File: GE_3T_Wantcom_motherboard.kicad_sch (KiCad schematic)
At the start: 27 parts, among them J1 Conn_01x03

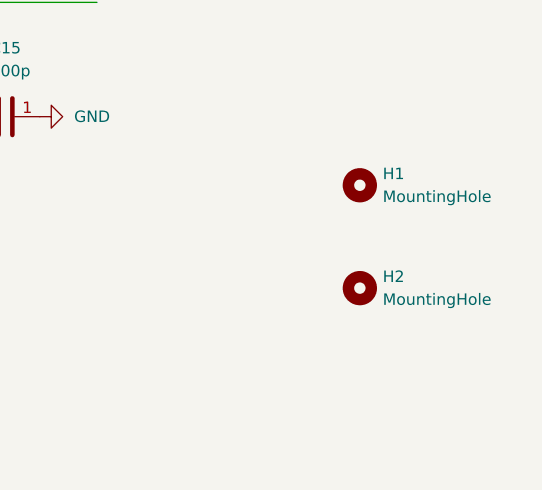
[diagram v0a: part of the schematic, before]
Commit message: board with screws, silkscreen issues
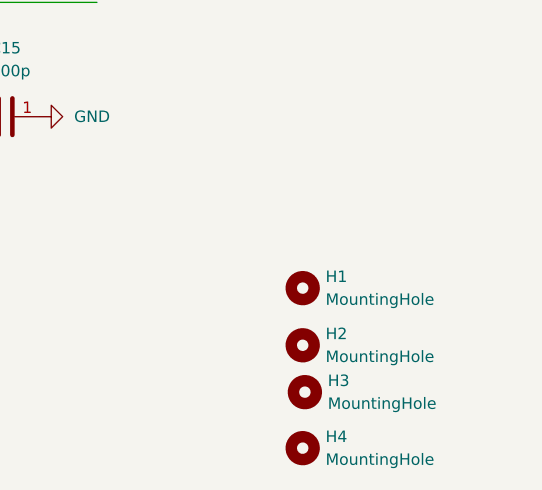
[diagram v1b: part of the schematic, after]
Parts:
- added H3, H4: MountingHole, aaa_MyLib:screw head 440, symbol Mechanical:MountingHole
- H1, H2: footprint (none) -> aaa_MyLib:screw head 440
- J1: footprint aaa_MyLib:CONN1_UFL-R_HIR -> aaa_UFL:CONN1_UFL-R_HIR
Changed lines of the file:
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@@
+    )
+  )
+  (symbol (lib_id "Mechanical:MountingHole") (at 199.39 123.19 0) (unit 1)
+    (in_bom yes) (on_board yes) (dnp no) (fields_autoplaced)
+    (property "Reference" "H1" (at 201.93 121.92 0)
+      (effects (font (size 1.27 1.27)) (justify left))
+    )
+    (property "Value" "MountingHole" (at 201.93 124.46 0)
+      (effects (font (size 1.27 1.27)) (justify left))
+    )
+    (property "Footprint" "aaa_MyLib:screw head 440" (at 199.39 123.19 0)
+      (effects (font (size 1.27 1.27)) hide)
+    )
+    (property "Datasheet" "~" (at 199.39 123.19 0)
+      (effects (font (size 1.27 1.27)) hide)
+    )
+    (instances
+      (project "GE_3T_Wantcom_motherboard"
+        (path "/459e52d8-2ec8-467a-85ef-a8f840b40177"
+          (reference "H1") (unit 1)
+        )
+      )
     )
   )
@@
     )
   )
+  (symbol (lib_id "Mechanical:MountingHole") (at 199.39 140.97 0) (unit 1)
+    (in_bom yes) (on_board yes) (dnp no) (fields_autoplaced)
+    (property "Reference" "H4" (at 201.93 139.7 0)
+      (effects (font (size 1.27 1.27)) (justify left))
+    )
+    (property "Value" "MountingHole" (at 201.93 142.24 0)
+      (effects (font (size 1.27 1.27)) (justify left))
+    )
+    (property "Footprint" "aaa_MyLib:screw head 440" (at 199.39 140.97 0)
+      (effects (font (size 1.27 1.27)) hide)
+    )
+    (property "Datasheet" "~" (at 199.39 140.97 0)
+      (effects (font (size 1.27 1.27)) hide)
+    )
+    (instances
+      (project "GE_3T_Wantcom_motherboard"
+        (path "/459e52d8-2ec8-467a-85ef-a8f840b40177"
+          (reference "H4") (unit 1)
+        )
+      )
+    )
+  )
   (symbol (lib_id "power:GND") (at 139.7 134.62 0) (unit 1)
     (in_bom yes) (on_board yes) (dnp no) (fields_autoplaced)
@@
       (effects (font (size 1.27 1.27)))
     )
-    (property "Footprint" "aaa_MyLib:CONN1_UFL-R_HIR" (at 38.1 93.98 0)
+    (property "Footprint" "aaa_UFL:CONN1_UFL-R_HIR" (at 38.1 93.98 0)
       (effects (font (size 1.27 1.27)) hide)
     )
@@
     )
   )
-  (symbol (lib_id "Mechanical:MountingHole") (at 205.74 111.76 0) (unit 1)
-    (in_bom yes) (on_board yes) (dnp no) (fields_autoplaced)
-    (property "Reference" "H1" (at 208.28 110.49 0)
-      (effects (font (size 1.27 1.27)) (justify left))
-    )
-    (property "Value" "MountingHole" (at 208.28 113.03 0)
-      (effects (font (size 1.27 1.27)) (justify left))
-    )
-    (property "Footprint" "" (at 205.74 111.76 0)
-      (effects (font (size 1.27 1.27)) hide)
-    )
-    (property "Datasheet" "~" (at 205.74 111.76 0)
-      (effects (font (size 1.27 1.27)) hide)
-    )
-    (instances
-      (project "GE_3T_Wantcom_motherboard"
-        (path "/459e52d8-2ec8-467a-85ef-a8f840b40177"
-          (reference "H1") (unit 1)
-        )
-      )
-    )
-  )
   (symbol (lib_id "AAA_MyLib:C_0603_1608metric") (at 102.87 133.35 180) (unit 1)
     (in_bom yes) (on_board yes) (dnp no) (fields_autoplaced)
@@
     )
   )
+  (symbol (lib_id "Mechanical:MountingHole") (at 199.39 129.54 0) (unit 1)
+    (in_bom yes) (on_board yes) (dnp no) (fields_autoplaced)
+    (property "Reference" "H2" (at 201.93 128.27 0)
+      (effects (font (size 1.27 1.27)) (justify left))
+    )
+    (property "Value" "MountingHole" (at 201.93 130.81 0)
+      (effects (font (size 1.27 1.27)) (justify left))
+    )
+    (property "Footprint" "aaa_MyLib:screw head 440" (at 199.39 129.54 0)
+      (effects (font (size 1.27 1.27)) hide)
+    )
+    (property "Datasheet" "~" (at 199.39 129.54 0)
+      (effects (font (size 1.27 1.27)) hide)
+    )
+    (instances
+      (project "GE_3T_Wantcom_motherboard"
+        (path "/459e52d8-2ec8-467a-85ef-a8f840b40177"
+          (reference "H2") (unit 1)
+        )
+      )
+    )
+  )
   (symbol (lib_id "AAA_MyLib:L_choke_1008_2520metric") (at 161.29 88.9 0) (unit 1)
     (in_bom yes) (on_board yes) (dnp no) (fields_autoplaced)
@@
     )
   )
-  (symbol (lib_id "Mechanical:MountingHole") (at 205.74 123.19 0) (unit 1)
-    (in_bom yes) (on_board yes) (dnp no) (fields_autoplaced)
-    (property "Reference" "H2" (at 208.28 121.92 0)
-      (effects (font (size 1.27 1.27)) (justify left))
-    )
-    (property "Value" "MountingHole" (at 208.28 124.46 0)
-      (effects (font (size 1.27 1.27)) (justify left))
-    )
-    (property "Footprint" "" (at 205.74 123.19 0)
-      (effects (font (size 1.27 1.27)) hide)
-    )
-    (property "Datasheet" "~" (at 205.74 123.19 0)
-      (effects (font (size 1.27 1.27)) hide)
-    )
-    (instances
-      (project "GE_3T_Wantcom_motherboard"
-        (path "/459e52d8-2ec8-467a-85ef-a8f840b40177"
-          (reference "H2") (unit 1)
-        )
-      )
+  (symbol (lib_id "Mechanical:MountingHole") (at 199.6334 134.7491 0) (unit 1)
+    (in_bom yes) (on_board yes) (dnp no) (fields_autoplaced)
+    (property "Reference" "H3" (at 202.1734 133.4791 0)
+      (effects (font (size 1.27 1.27)) (justify left))
+    )
+    (property "Value" "MountingHole" (at 202.1734 136.0191 0)
+      (effects (font (size 1.27 1.27)) (justify left))
+    )
+    (property "Footprint" "aaa_MyLib:screw head 440" (at 199.6334 134.7491 0)
+      (effects (font (size 1.27 1.27)) hide)
+    )
+    (property "Datasheet" "~" (at 199.6334 134.7491 0)
+      (effects (font (size 1.27 1.27)) hide)
+    )
+    (instances
+      (project "GE_3T_Wantcom_motherboard"
+        (path "/459e52d8-2ec8-467a-85ef-a8f840b40177"
+          (reference "H3") (unit 1)
+        )
+      )
